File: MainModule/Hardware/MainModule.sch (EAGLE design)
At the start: 9 parts, among them U1 ULN2803ADW, U2 ULN2803ADW, U3 ULN2803ADW, X1 MKDSN1,5/8-5,08, X2 MKDSN1,5/8-5,08, X3 MKDSN1,5/8-5,08, X4 MKDSN1,5/2-5,08, X5 MKDSN1,5/3-5,08

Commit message: 80% of the PCB design is ready.
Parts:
- added R1, R2: 10K, rcl:R-EU_MELF0204W
- added X6, X7: 057-016-0, con-panduit:057-016-0
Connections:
- new net N$49: LPC1.42, X6-2.S
- new net N$50: LPC1.47, X6-12.S
- new net N$51: LPC1.46, X6-10.S
- new net N$52: LPC1.45, X6-8.S
- new net N$53: LPC1.44, X6-6.S
- new net N$54: LPC1.53, X6-16.S
- new net N$55: LPC1.52, X6-14.S
- new net N$56: LPC1.43, X6-4.S
- new net N$57: LPC1.69, X7-14.S
- new net N$58: LPC1.70, X7-12.S
- new net N$59: LPC1.67, X7-10.S
- new net N$60: LPC1.64, X7-8.S
- new net N$61: LPC1.68, X7-16.S
- new net N$62: LPC1.61, X7-6.S
- new net N$63: LPC1.58, X7-4.S
- new net N$64: LPC1.55, X7-2.S
- new net SCL1: LPC1.56, X7-3.S
- new net SCL2: LPC1.41, R1.2, X6-3.S
- new net SDA1: LPC1.57, X7-5.S
- new net SDA2: LPC1.40, R2.2, X6-5.S
- new net VCC: LPC1.2, R1.1, R2.1, X6-1.S, X7-1.S
- net GND: now also X6-15.S, X7-15.S
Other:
- moved on the sheet: LPC1, U1, U2, U3, X1-1, X1-2, X1-3, X1-4, X1-5, X1-6, X1-7, X1-8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

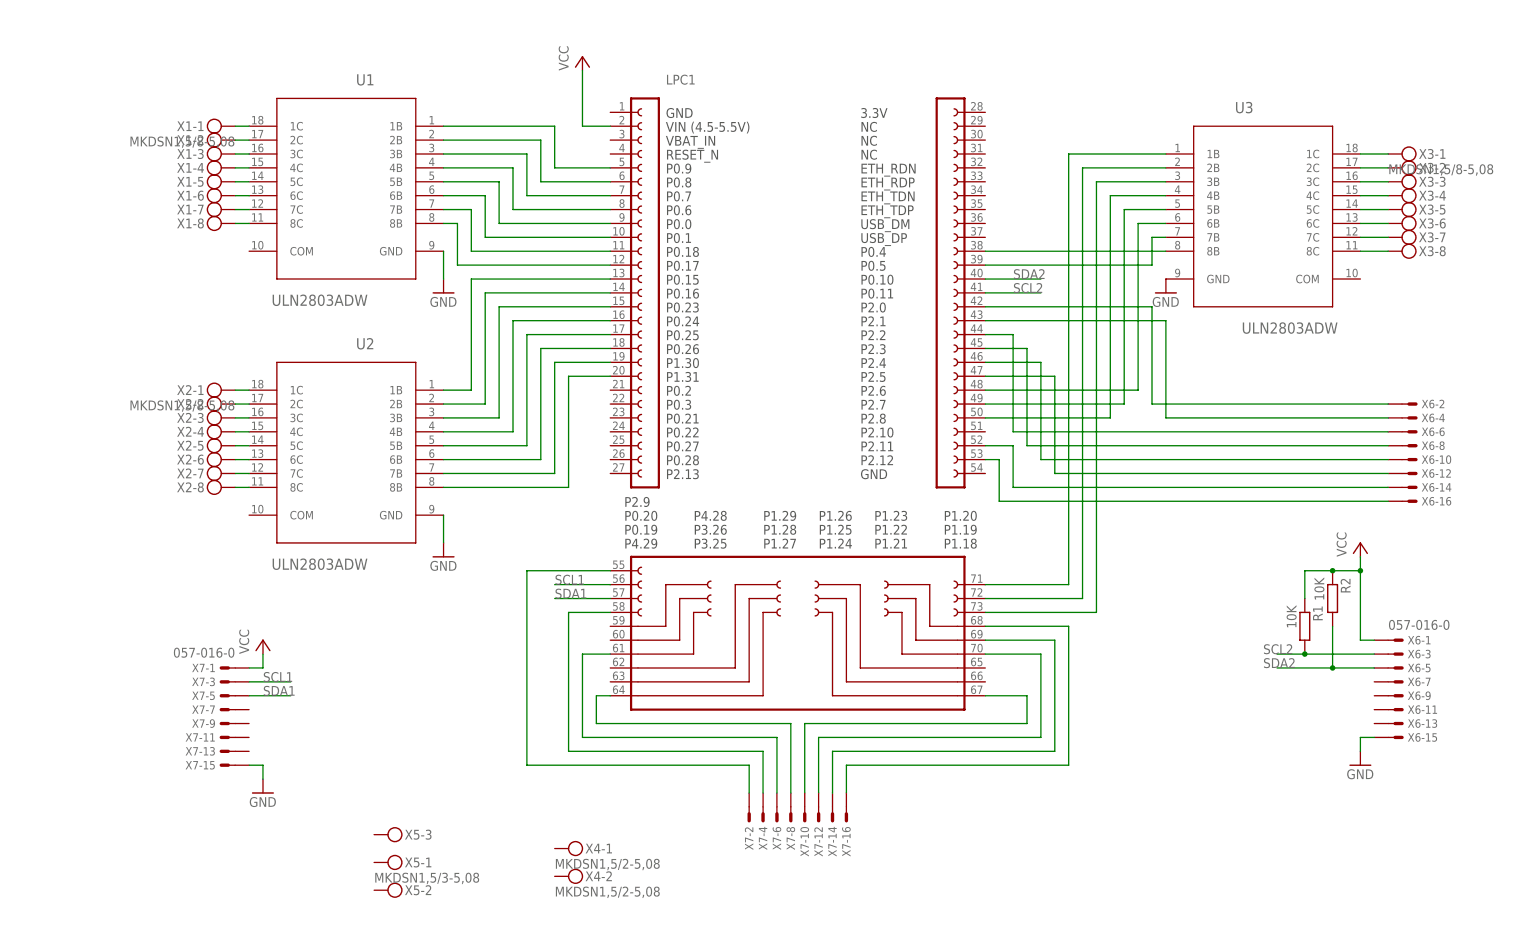
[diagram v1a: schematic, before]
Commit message: 95% of PCB design is ready. (Added linear regulator)
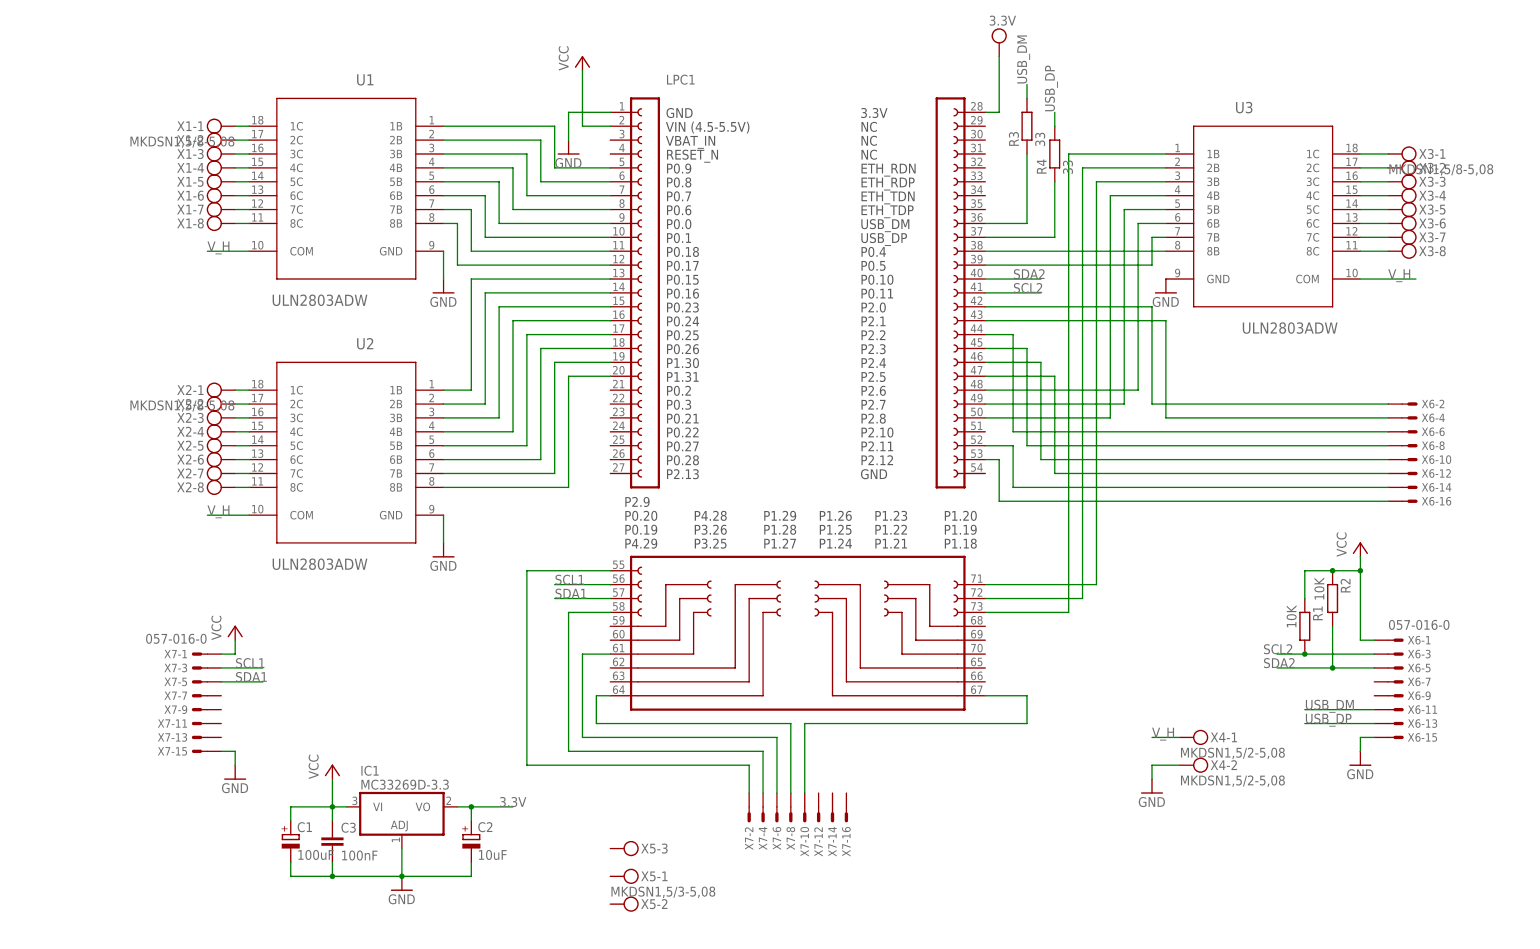
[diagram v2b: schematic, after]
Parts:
- added C1: 100uF, rcl:CPOL-EU153CLV-0810
- added C2: 10uF, rcl:CPOL-EU153CLV-0810
- added C3: 100nF, rcl:C-EUC0805
- added IC1: MC33269D-3.3, linear:MC33269D-3.3
- added R3, R4: 33, resistor:R-EU_M3216
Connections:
- removed net N$22: LPC1.73, U3.3B
- removed net N$57 (its old number): LPC1.69, X7-14.S
- removed net N$58: LPC1.70, X7-12.S
- removed net N$61: LPC1.68, X7-16.S
- new net 3.3V: C2.+, IC1.VO, LPC1.28
- new net N$65: LPC1.36, R3.1
- new net N$66: LPC1.37, R4.1
- new net N$69: LPC1.71, U3.3B
- new net USB_DM: R3.2, X6-11.S
- new net USB_DP: R4.2, X6-13.S
- new net V_H: U1.COM, U2.COM, U3.COM, X4-1.KL
- net GND: now also C1.-, C2.-, C3.2, IC1.ADJ, LPC1.1, X4-2.KL
- net N$24: now also LPC1.73; no longer LPC1.71
- net VCC: now also C1.+, C3.1, IC1.VI
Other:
- moved on the sheet: X4-1, X4-2, X5-1, X5-2, X5-3, X7-1, X7-11, X7-13, X7-15, X7-3, X7-5, X7-7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

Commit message: Reduce number of outputs and increase power of each of them.
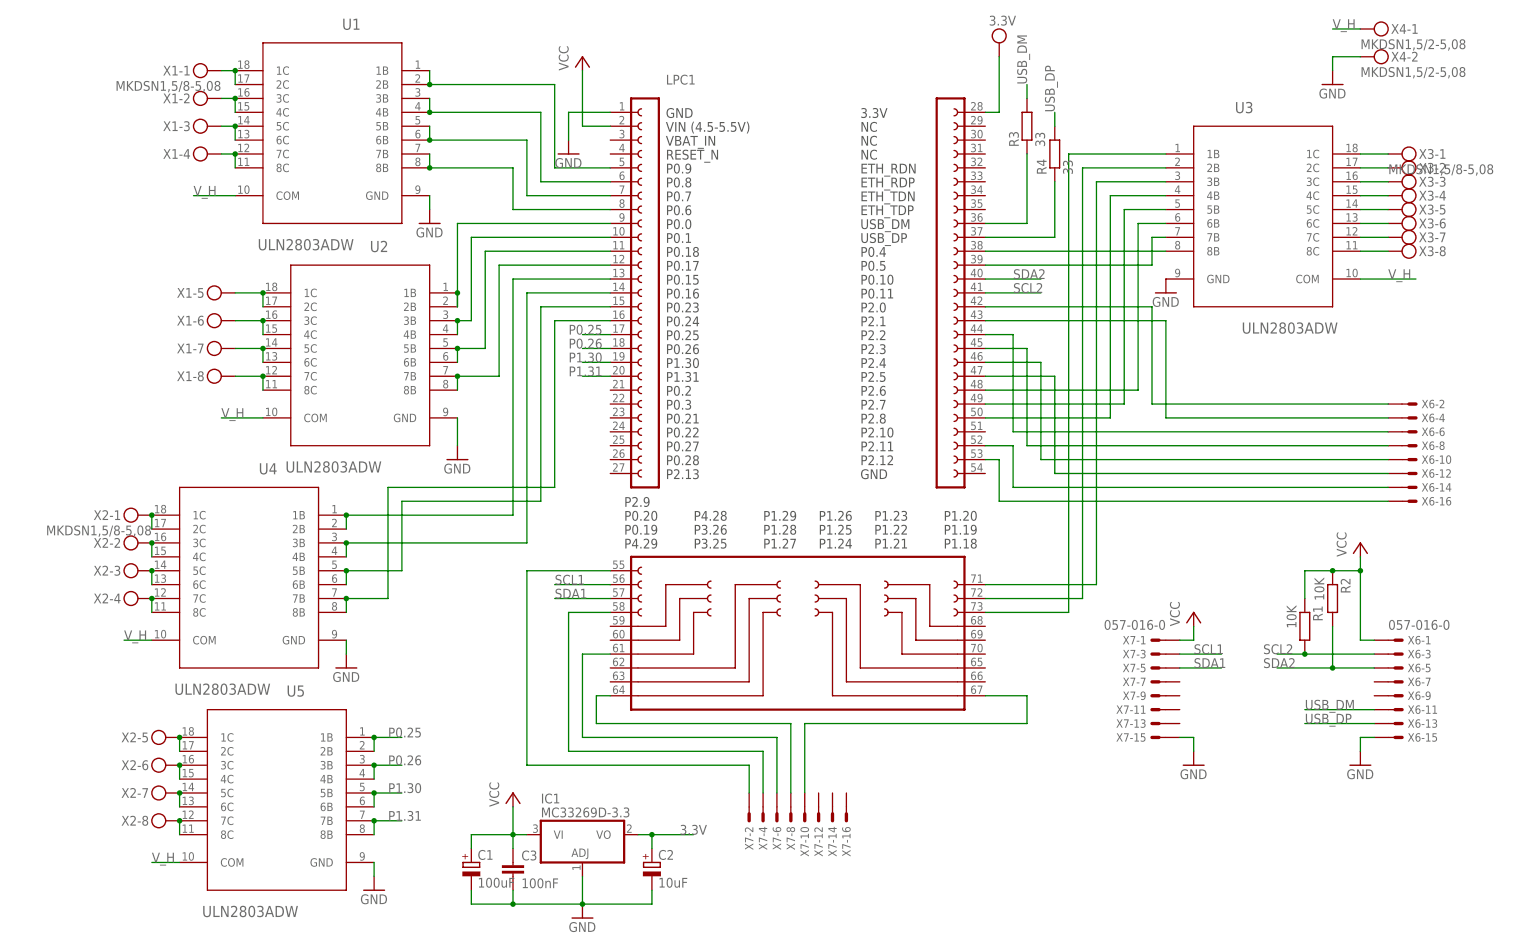
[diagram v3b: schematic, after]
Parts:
- removed X5: MKDSN1,5/3-5,08, con-phoenix-508:MKDSN1,5/3-5,08
- added U4, U5: ULN2803ADW, ULN2803:ULN2803ADW
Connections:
- removed net N$35: U2.3C, X2-3.KL
- removed net N$36: U2.4C, X2-4.KL
- removed net N$37: U2.5C, X2-5.KL
- removed net N$38: U2.6C, X2-6.KL
- removed net N$39: U2.7C, X2-7.KL
- removed net N$40: U2.8C, X2-8.KL
- new net N$22: U1.3C, U1.4C, X1-2.KL
- new net N$23: U1.5C, U1.6C, X1-3.KL
- new net P0.25: LPC1.17, U5.1B, U5.2B
- new net P0.26: LPC1.18, U5.3B, U5.4B
- new net P1.30: LPC1.19, U5.5B, U5.6B
- new net P1.31: LPC1.20, U5.7B, U5.8B
- net GND: now also U4.GND, U5.GND
- net N$1: now also U1.2B
- net N$10: now also U4.3B, U4.4B; no longer U2.2B
- net N$11: now also U4.5B, U4.6B; no longer U2.3B
- net N$12: now also U4.7B, U4.8B; no longer U2.4B
- net N$13: now also U5.1C, U5.2C, X2-5.KL; no longer LPC1.17, U2.5B
- net N$14: now also U5.3C, U5.4C, X2-6.KL; no longer LPC1.18, U2.6B
- net N$15: now also U2.1C, U2.2C, X1-5.KL; no longer LPC1.19, U2.7B
- net N$16: now also U5.5C, U5.6C, X2-7.KL; no longer LPC1.20, U2.8B
- net N$2: now also U1.3B, U1.4B; no longer U1.2B
- net N$25: now also U1.2C
- net N$26: now also U1.7C, U1.8C, X1-4.KL; no longer U1.2C, X1-2.KL
- net N$27: now also U5.7C, U5.8C, X2-8.KL; no longer U1.3C, X1-3.KL
- net N$28: now also U2.3C, U2.4C, X1-6.KL; no longer U1.4C, X1-4.KL
- net N$29: now also U2.5C, U2.6C, X1-7.KL; no longer U1.5C, X1-5.KL
- net N$3: now also U1.5B, U1.6B; no longer U1.3B
- net N$30: now also U2.7C, U2.8C, X1-8.KL; no longer U1.6C, X1-6.KL
- net N$31: now also U4.1C, U4.2C, X2-1.KL; no longer U1.7C, X1-7.KL
- net N$32: now also U4.3C, U4.4C, X2-2.KL; no longer U1.8C, X1-8.KL
- net N$33: now also U4.5C, U4.6C, X2-3.KL; no longer U2.1C, X2-1.KL
- net N$34: now also U4.7C, U4.8C, X2-4.KL; no longer U2.2C, X2-2.KL
- net N$4: now also U1.7B, U1.8B; no longer U1.4B
- net N$5: now also U2.1B, U2.2B; no longer U1.5B
- net N$6: now also U2.3B, U2.4B; no longer U1.6B
- net N$7: now also U2.5B, U2.6B; no longer U1.7B
- net N$8: now also U2.7B, U2.8B; no longer U1.8B
- net N$9: now also U4.1B, U4.2B; no longer U2.1B
- net V_H: now also U4.COM, U5.COM
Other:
- moved on the sheet: C1, C2, C3, IC1, U1, U2, X1-1, X1-2, X1-3, X1-4, X1-5, X1-6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

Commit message: Dodadeni LED za signalizacija na aktiven izlez
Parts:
- added LED1, LED10, LED11, LED12, LED13, LED14, LED15, LED16, LED2, LED3, LED4, LED5, LED6, LED7, LED8, LED9: Blue, led:LEDCHIPLED_0805
- added R10, R11, R12, R13, R14, R15, R16, R17, R18, R19, R20, R5, R6, R7, R8, R9: 133, rcl:R-EU_R1206W
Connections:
- removed net N$10: LPC1.14, U4.3B, U4.4B
- removed net N$11: LPC1.15, U4.5B, U4.6B
- removed net N$12: LPC1.16, U4.7B, U4.8B
- removed net N$5: LPC1.9, U2.1B, U2.2B
- removed net N$6: LPC1.10, U2.3B, U2.4B
- removed net N$7: LPC1.11, U2.5B, U2.6B
- removed net N$8: LPC1.12, U2.7B, U2.8B
- removed net N$9: LPC1.13, U4.1B, U4.2B
- new net N$35: LED1.A, R5.1
- new net N$36: LED2.A, R6.1
- new net N$37: LED3.A, R7.1
- new net N$38: LED4.A, R8.1
- new net N$39: LED5.A, R9.1
- new net N$40: LED6.A, R10.1
- new net N$58: LED7.A, R11.1
- new net N$59: LED8.A, R12.1
- new net N$61: LED9.A, R13.1
- new net N$67: LED10.A, R14.1
- new net N$70: LED11.A, R15.1
- new net N$71: LED12.A, R16.1
- new net OUT1: LPC1.5, R5.2, U1.1B, U1.2B
- new net OUT10: LPC1.14, R14.2, U4.3B, U4.4B
- new net OUT11: LPC1.15, R15.2, U4.5B, U4.6B
- new net OUT12: LPC1.16, R16.2, U4.7B, U4.8B
- new net OUT2: LPC1.6, R6.2, U1.3B, U1.4B
- new net OUT3: LPC1.7, R7.2, U1.5B, U1.6B
- new net OUT4: LPC1.8, R8.2, U1.7B, U1.8B
- new net OUT5: LPC1.9, R9.2, U2.1B, U2.2B
- new net OUT6: LPC1.10, R10.2, U2.3B, U2.4B
- new net OUT7: LPC1.11, R11.2, U2.5B, U2.6B
- new net OUT8: LPC1.12, R12.2, U2.7B, U2.8B
- new net OUT9: LPC1.13, R13.2, U4.1B, U4.2B
- net GND: now also LED1.C, LED10.C, LED11.C, LED12.C, LED13.C, LED14.C, LED15.C, LED16.C, LED2.C, LED3.C, LED4.C, LED5.C, LED6.C, LED7.C, LED8.C, LED9.C
- net N$1: now also LED15.A, R19.1; no longer LPC1.5, U1.1B, U1.2B
- net N$2: now also LED13.A, R17.1; no longer LPC1.6, U1.3B, U1.4B
- net N$3: now also LED14.A, R18.1; no longer LPC1.7, U1.5B, U1.6B
- net N$4: now also LED16.A, R20.1; no longer LPC1.8, U1.7B, U1.8B
- net P0.25: now also R17.2
- net P0.26: now also R18.2
- net P1.30: now also R19.2
- net P1.31: now also R20.2
